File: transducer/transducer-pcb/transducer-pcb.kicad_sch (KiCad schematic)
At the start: 14 parts, among them J1 Load Cell, J2 Sheild, J3 RJ45, J4 AMP RIGHT, J5 AMP LEFT, J6 NANO UR, J7 NANO LR, J8 NANO UL, J9 NANO LL

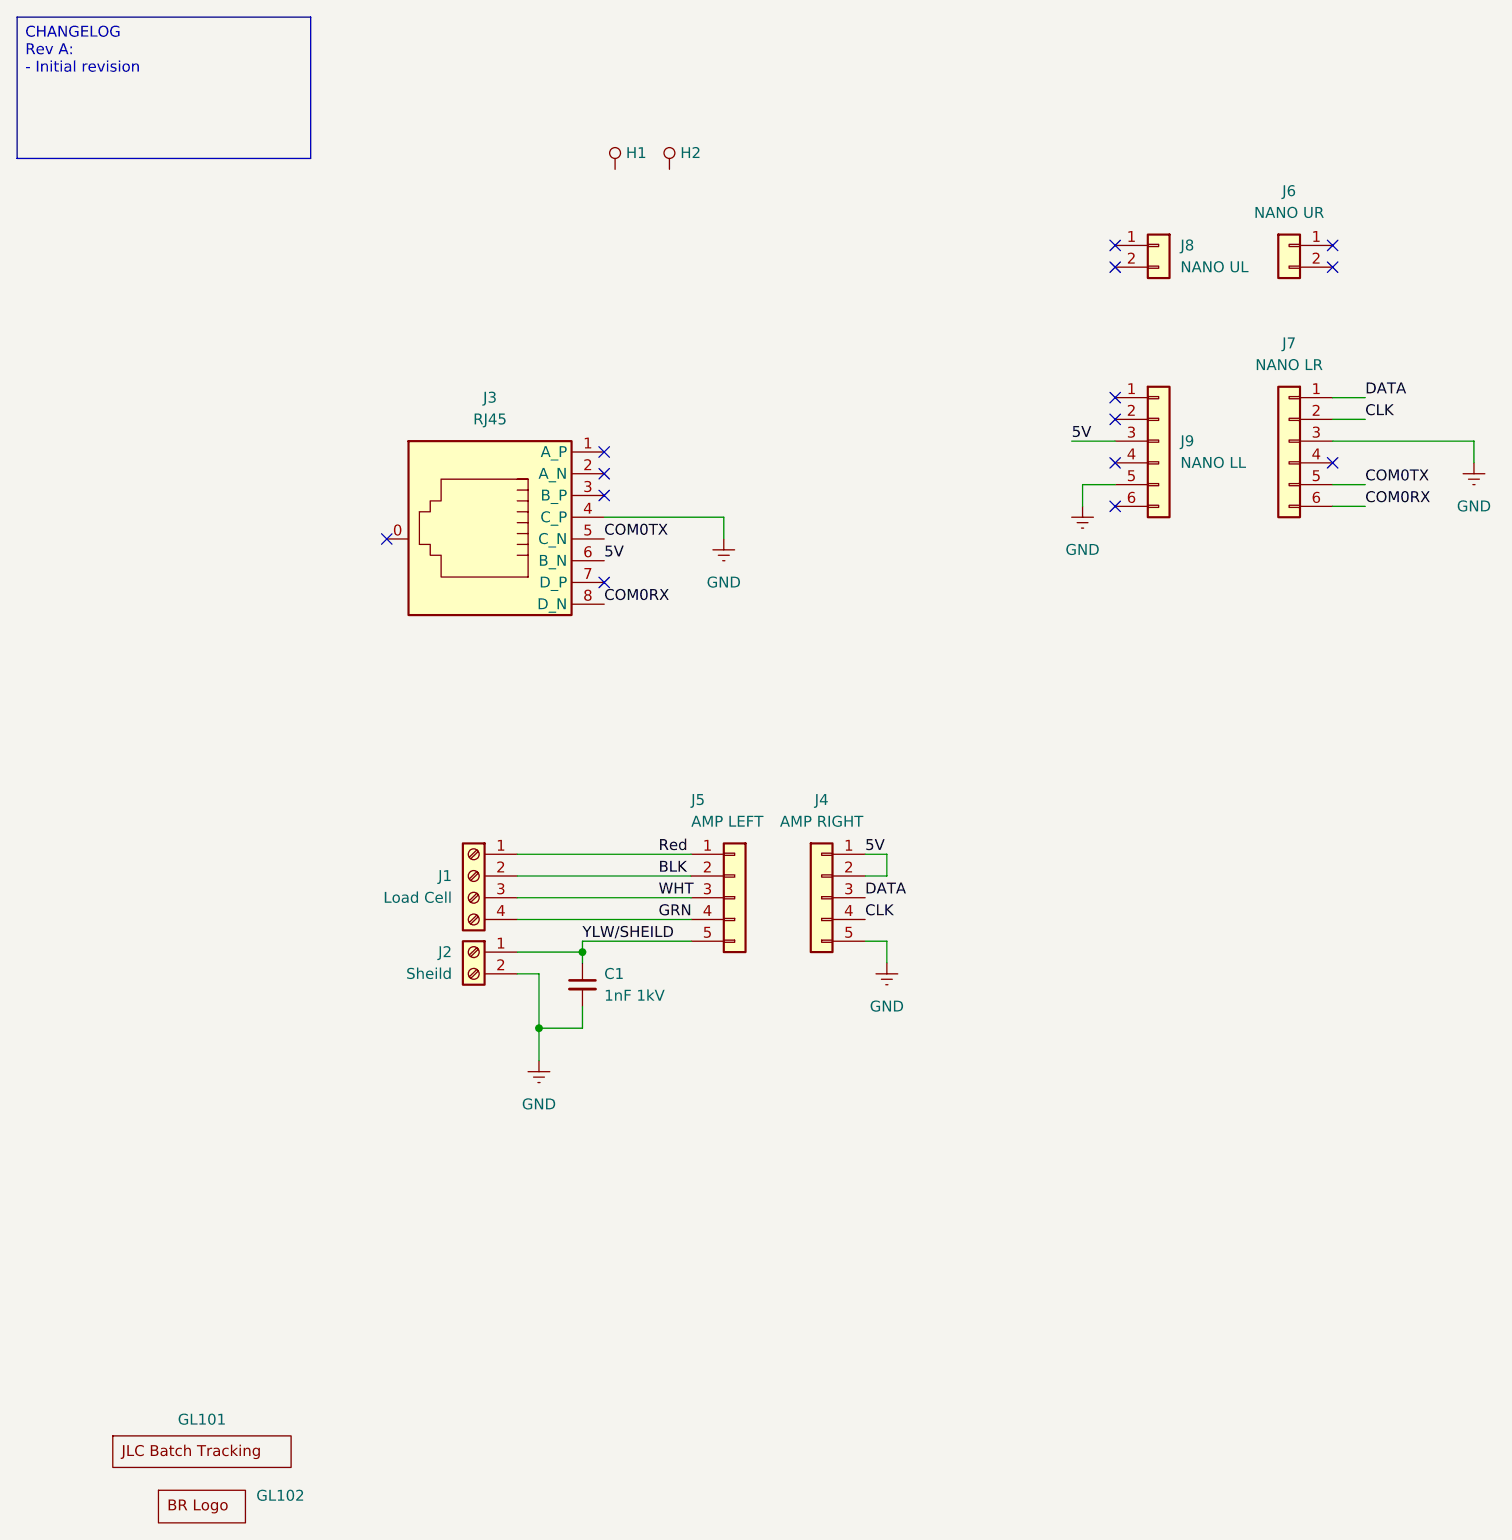
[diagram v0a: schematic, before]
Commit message: Rev B PCBA and move arduino file to folder
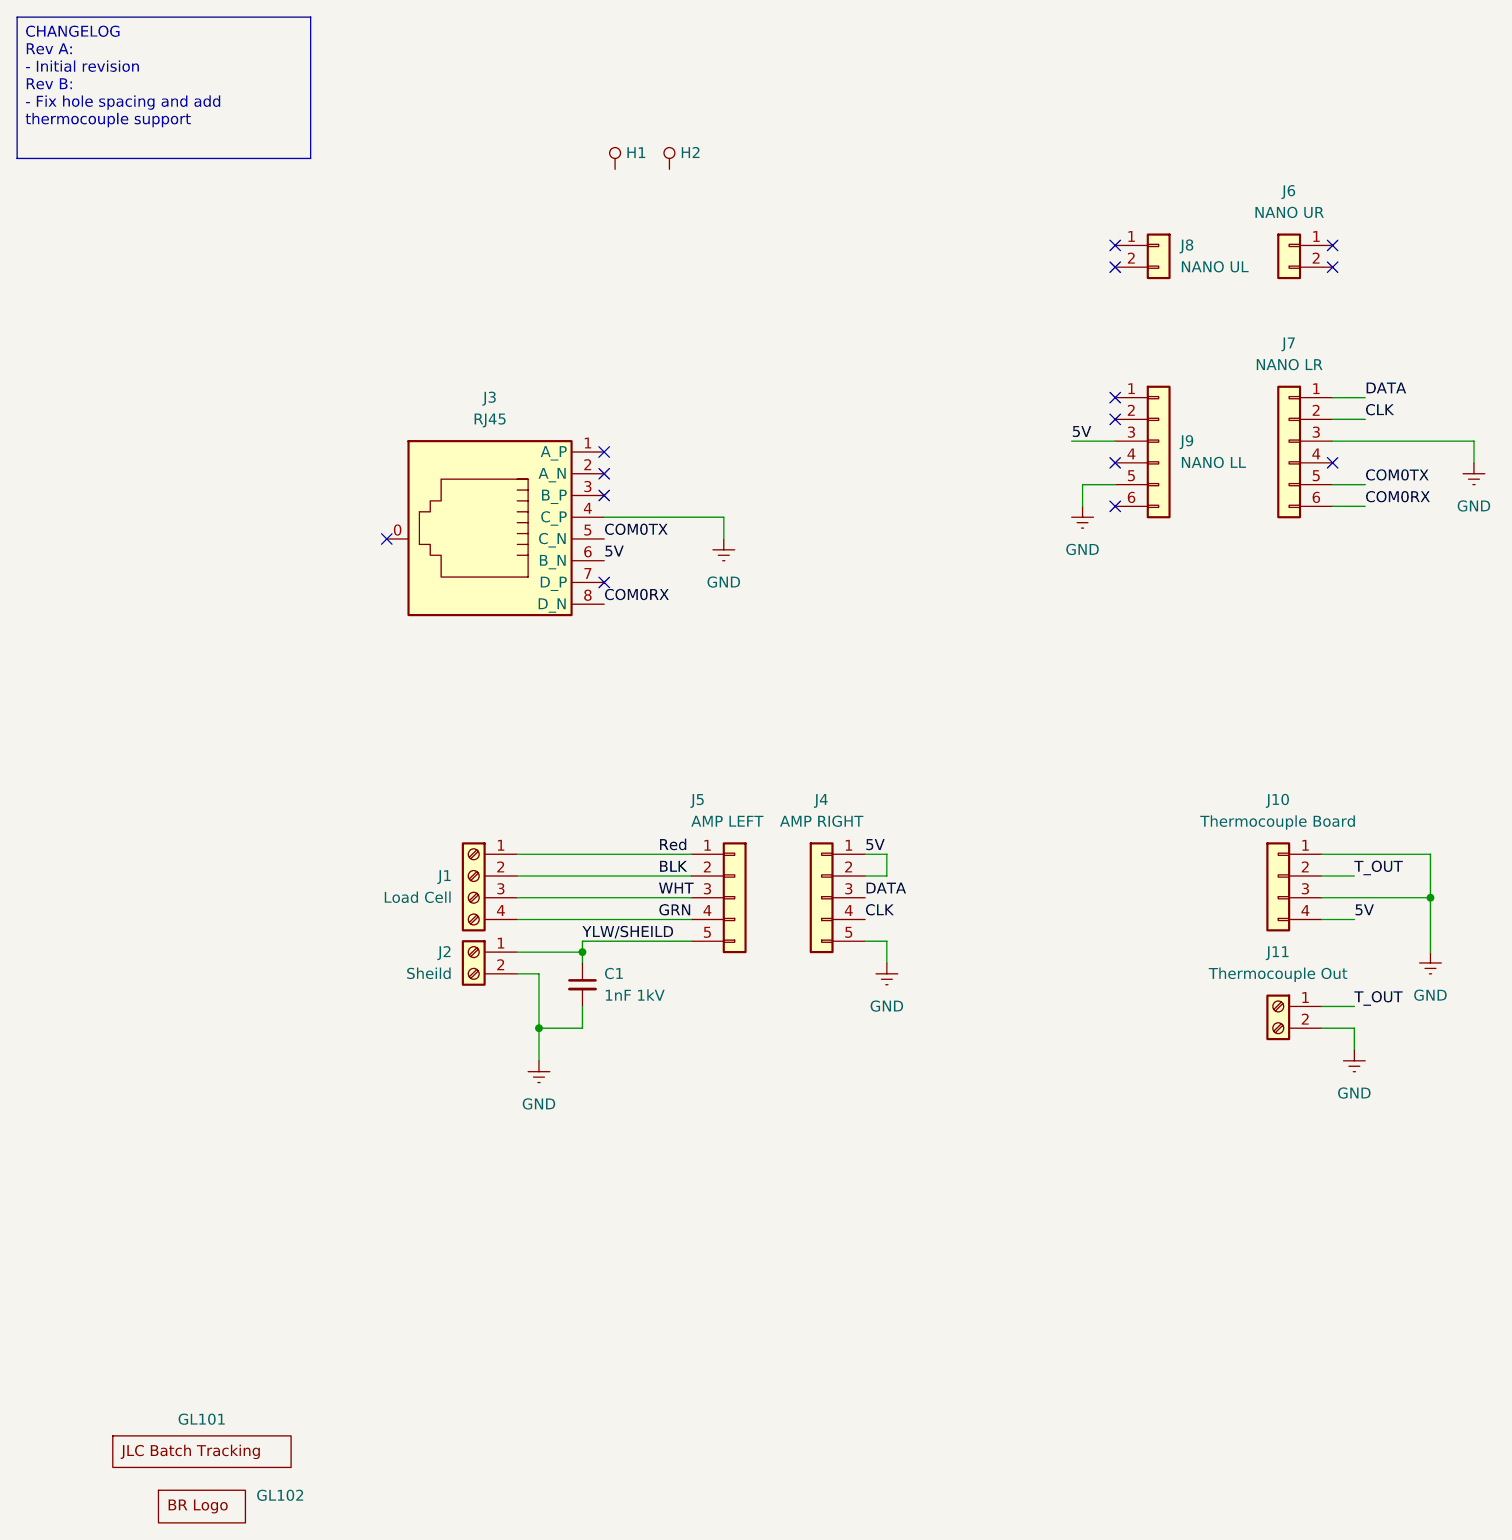
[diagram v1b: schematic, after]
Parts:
- added J10: Thermocouple Board, BR_Connectors:Pin_Header_1x4_2.54mm_Vertical, symbol BR_Connectors_Header:Header_Pin_01x04_2.54mm_Vert_PTH
- added J11: Thermocouple Out, BR_Connectors:KF128-2.54-2P, symbol BR_Connectors:KF128-2.54-2P
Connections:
- net 5V: now also J10.4 (Pin_4)
- net GND: now also J10.1 (Pin_1), J10.3 (Pin_3), J11.2 (Pin_2)
- new net T_OUT: J10.2 (Pin_2), J11.1 (Pin_1)
